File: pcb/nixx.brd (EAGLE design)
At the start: 20 x 40 mm, 42 parts

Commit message: added eeprom
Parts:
- added IC1: 24C64ST, joyAnalog:TSSOP8
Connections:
- new net VCC: IC1.8
- net GND: now also IC1.4
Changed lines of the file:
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@@
 <grid distance="5" unitdist="mil" unit="mm" style="lines" multiple="1" display="no" altdistance="1" altunitdist="mil" altunit="mil"/>
 <layers>
-<layer number="1" name="Top" color="4" fill="1" visible="yes" active="yes"/>
+<layer number="1" name="Top" color="4" fill="1" visible="no" active="yes"/>
 <layer number="16" name="Bottom" color="1" fill="1" visible="yes" active="yes"/>
 <layer number="17" name="Pads" color="2" fill="1" visible="yes" active="yes"/>
@@
 <layer number="21" name="tPlace" color="7" fill="1" visible="yes" active="yes"/>
 <layer number="22" name="bPlace" color="7" fill="1" visible="yes" active="yes"/>
-<layer number="23" name="tOrigins" color="15" fill="1" visible="yes" active="yes"/>
+<layer number="23" name="tOrigins" color="15" fill="1" visible="no" active="yes"/>
 <layer number="24" name="bOrigins" color="15" fill="1" visible="yes" active="yes"/>
-<layer number="25" name="tNames" color="7" fill="1" visible="yes" active="yes"/>
+<layer number="25" name="tNames" color="7" fill="1" visible="no" active="yes"/>
 <layer number="26" name="bNames" color="7" fill="1" visible="yes" active="yes"/>
-<layer number="27" name="tValues" color="7" fill="1" visible="yes" active="yes"/>
+<layer number="27" name="tValues" color="7" fill="1" visible="no" active="yes"/>
 <layer number="28" name="bValues" color="7" fill="1" visible="yes" active="yes"/>
 <layer number="29" name="tStop" color="7" fill="3" visible="no" active="yes"/>
@@
 <layer number="49" name="Reference" color="7" fill="1" visible="yes" active="yes"/>
 <layer number="50" name="dxf" color="7" fill="1" visible="yes" active="yes"/>
-<layer number="51" name="tDocu" color="7" fill="1" visible="yes" active="yes"/>
+<layer number="51" name="tDocu" color="7" fill="1" visible="no" active="yes"/>
 <layer number="52" name="bDocu" color="7" fill="1" visible="yes" active="yes"/>
 <layer number="53" name="tGND_GNDA" color="7" fill="1" visible="yes" active="yes"/>
@@
 <attribute name="VALUE" x="7.239" y="10.287" size="0.4064" layer="28" rot="MR180"/>
 </element>
+<element name="IC1" library="joyAnalog" package="TSSOP8" value="24C64ST" x="9.398" y="8.509" rot="MR0">
+<attribute name="MPN" value="CAT24C64YI-GT3" x="9.398" y="8.509" size="1.778" layer="28" rot="MR0" display="off"/>
+<attribute name="OC_FARNELL" value="1718133" x="9.398" y="8.509" size="1.778" layer="28" rot="MR0" display="off"/>
+<attribute name="OC_NEWARK" value="08R5418" x="9.398" y="8.509" size="1.778" layer="28" rot="MR0" display="off"/>
+<attribute name="MF" value="" x="9.398" y="8.509" size="1.778" layer="28" rot="MR0" display="off"/>
+</element>
 </elements>
 <signals>
@@
 <wire x1="9.155" y1="8.89" x2="10.171" y2="7.874" width="0.2032" layer="16"/>
 <wire x1="10.171" y1="7.874" x2="10.414" y2="7.874" width="0.2032" layer="16"/>
+<contactref element="IC1" pad="4"/>
+<wire x1="10.171" y1="7.874" x2="8.423" y2="5.584" width="0" layer="19" extent="16-16"/>
 </signal>
 <signal name="N$1">
@@
 <wire x1="0.7366" y1="34.6456" x2="1.27" y2="34.1122" width="0.2032" layer="1"/>
 <wire x1="1.27" y1="34.1122" x2="1.27" y2="33.412" width="0.2032" layer="1"/>
+<wire x1="7.355" y1="8.89" x2="12.573" y2="8.255" width="0" layer="19" extent="16-16"/>
 </signal>
 <signal name="SPI_SCK">
@@
 <wire x1="4.215" y1="11.581" x2="5.7074" y2="11.581" width="0.2032" layer="1"/>
 </signal>
+<signal name="VCC">
+<contactref element="IC1" pad="8"/>
+</signal>
 </signals>

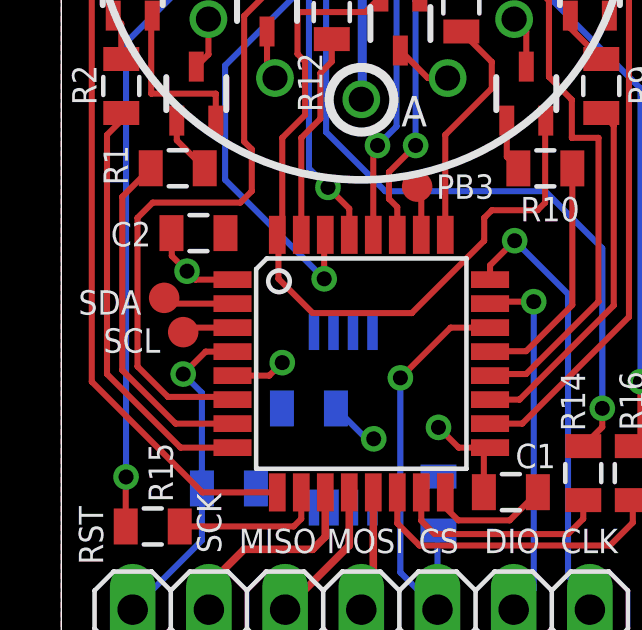
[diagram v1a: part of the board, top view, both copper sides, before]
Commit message: added eeprom
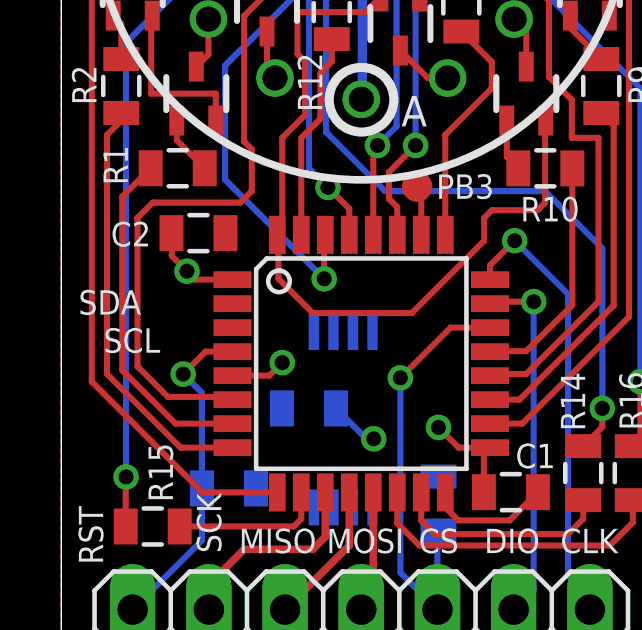
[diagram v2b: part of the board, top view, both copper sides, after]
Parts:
- removed TP1, TP2: TEST-POINT3X4, joyAnalog:PAD.03X.04
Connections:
- removed net N$16: TP1.P$1, U$2.2
- removed net N$18: TP2.P$1, U$2.3
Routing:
- net N$16: track 2.36 -> 0.00 mm
- net N$18: track 1.71 -> 0.00 mm
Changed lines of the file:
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@@
 <attribute name="VALUE" x="17.653" y="7.747" size="0.4064" layer="27" rot="R270"/>
 </element>
-<element name="TP1" library="joyAnalog" package="PAD.03X.04" value="TEST-POINT3X4" x="3.429" y="12.573" smashed="yes"/>
-<element name="TP2" library="joyAnalog" package="PAD.03X.04" value="TEST-POINT3X4" x="4.064" y="11.43" smashed="yes"/>
 <element name="TP3" library="joyAnalog" package="PAD.03X.04" value="TEST-POINT3X4" x="11.8618" y="16.2814" smashed="yes"/>
 <element name="R17" library="joyAnalog" package="0805" value="" x="5.588" y="6.223" smashed="yes" rot="MR180">
@@
 <wire x1="10.795" y1="16.129" x2="8.8265" y2="18.0975" width="0.2032" layer="16"/>
 </signal>
-<signal name="N$16">
-<contactref element="TP1" pad="P$1"/>
-<contactref element="U$2" pad="2"/>
-<wire x1="5.7074" y1="12.381" x2="3.621" y2="12.381" width="0.2032" layer="1"/>
-<wire x1="3.621" y1="12.381" x2="3.429" y2="12.573" width="0.2032" layer="1"/>
-</signal>
-<signal name="N$18">
-<contactref element="TP2" pad="P$1"/>
-<contactref element="U$2" pad="3"/>
-<wire x1="4.064" y1="11.43" x2="4.215" y2="11.581" width="0.2032" layer="1"/>
-<wire x1="4.215" y1="11.581" x2="5.7074" y2="11.581" width="0.2032" layer="1"/>
-</signal>
 <signal name="VCC">

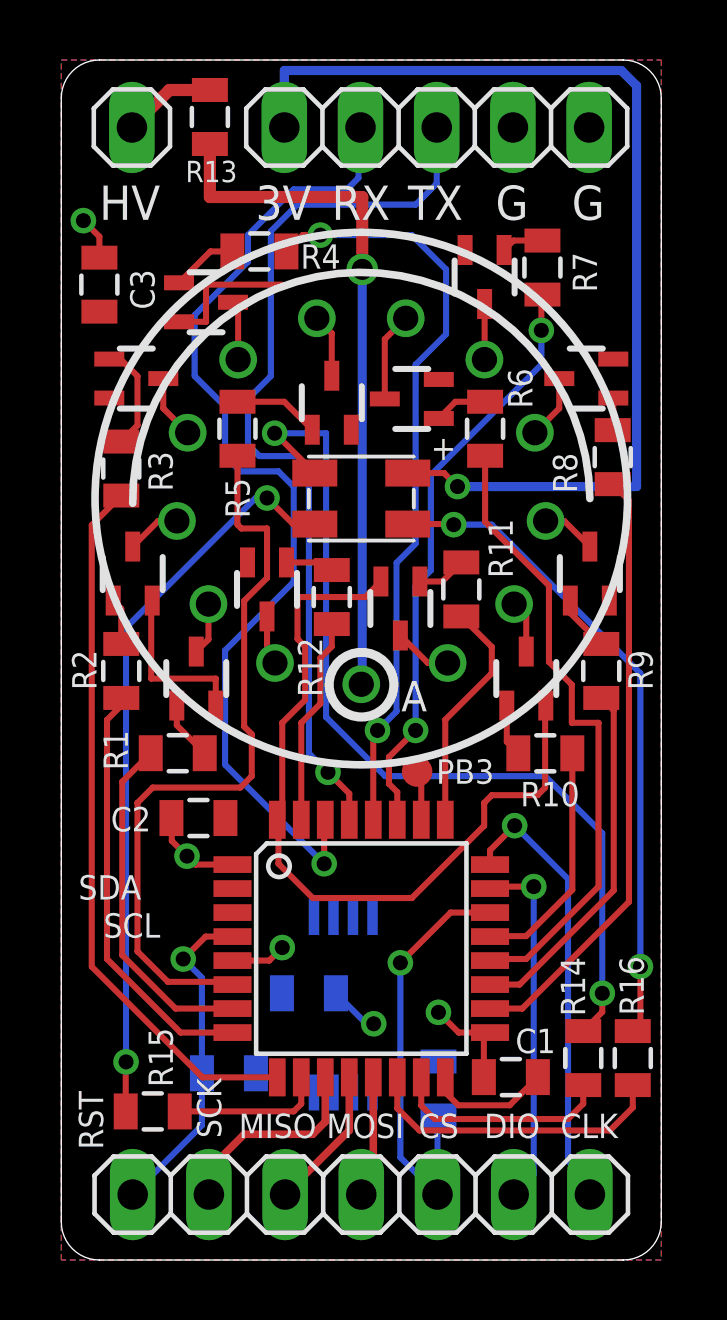
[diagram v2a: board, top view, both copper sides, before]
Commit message: added eeprom
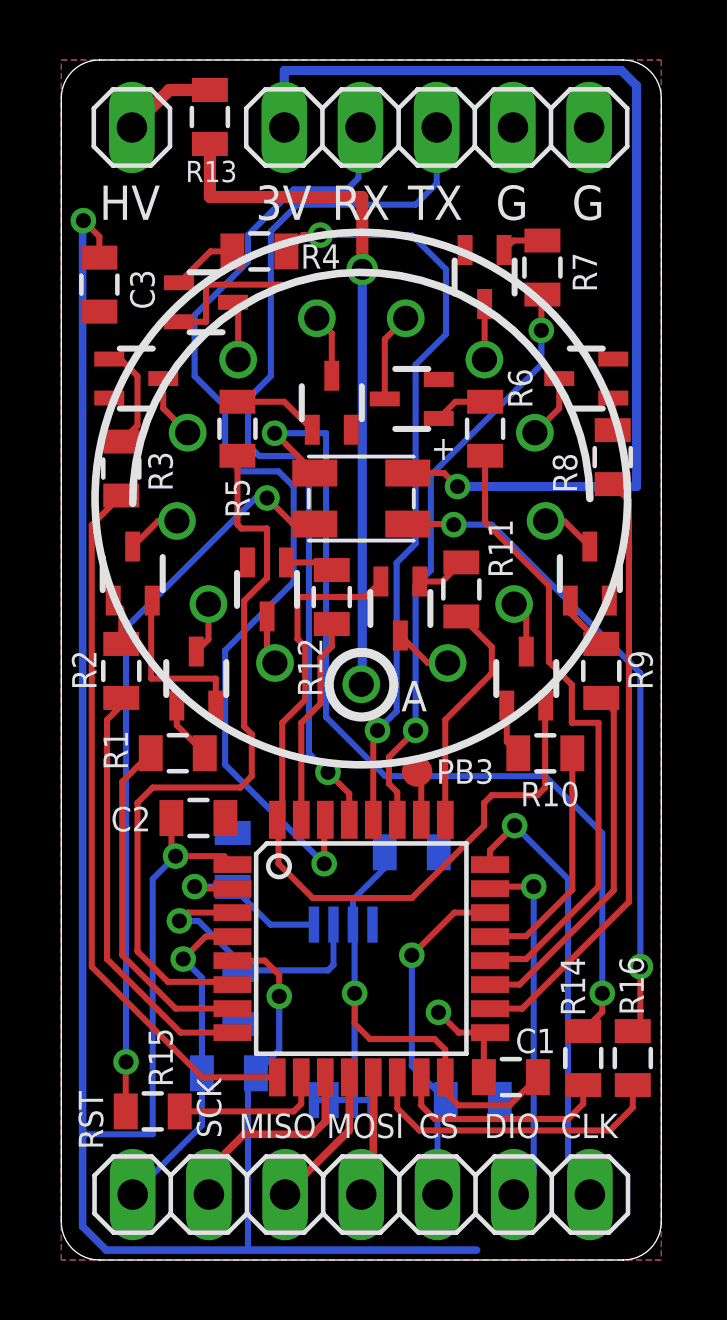
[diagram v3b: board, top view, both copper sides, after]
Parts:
- added R19, R20: (no value), joyAnalog:0805
- moved C4 5.82 mm to (11.7, 13.6), turned to 0 degrees
- moved R18 1.20 mm to (13.7, 5.33), turned to 180 degrees
- moved IC1 0.25 mm to (9.40, 8.26)
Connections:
- removed net VCC: IC1.8
- new net N$16: IC1.5, R20.1, U$2.2
- new net N$18: IC1.6, R19.1, U$2.3
- net +3V3: now also IC1.8, R19.2, R20.2
- net GND: now also IC1.1, IC1.2, IC1.3, IC1.7
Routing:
- net +3V3: track 45.0 -> 113.8 mm
- net GND: track 42.7 -> 57.0 mm
- net N$18: track 0.00 -> 9.27 mm, vias 0 -> 1
- net N$16: track 0.00 -> 5.99 mm, vias 0 -> 1
- net SPI_CS: track 14.6 -> 11.8 mm
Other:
- board text removed: "SCL"
- board text removed: "SDA"

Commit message: added eeprom
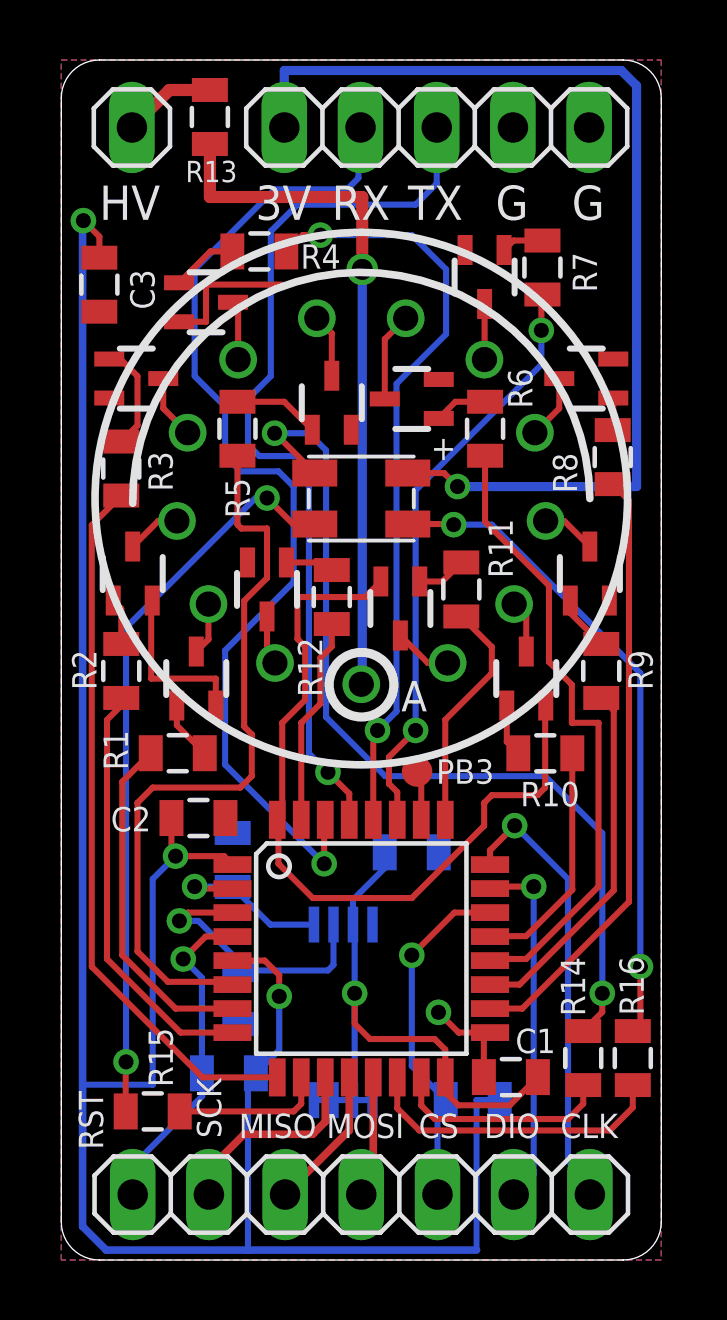
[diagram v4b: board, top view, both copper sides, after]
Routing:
- net +3V3: track 113.8 -> 117.9 mm
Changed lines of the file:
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@@
 <grid distance="5" unitdist="mil" unit="mil" style="lines" multiple="1" display="no" altdistance="1" altunitdist="mil" altunit="mil"/>
 <layers>
-<layer number="1" name="Top" color="4" fill="1" visible="no" active="yes"/>
+<layer number="1" name="Top" color="4" fill="1" visible="yes" active="yes"/>
 <layer number="16" name="Bottom" color="1" fill="1" visible="yes" active="yes"/>
 <layer number="17" name="Pads" color="2" fill="1" visible="yes" active="yes"/>
@@
 <layer number="19" name="Unrouted" color="6" fill="1" visible="yes" active="yes"/>
 <layer number="20" name="Dimension" color="15" fill="1" visible="yes" active="yes"/>
-<layer number="21" name="tPlace" color="7" fill="1" visible="yes" active="yes"/>
+<layer number="21" name="tPlace" color="7" fill="1" visible="no" active="yes"/>
 <layer number="22" name="bPlace" color="7" fill="1" visible="yes" active="yes"/>
 <layer number="23" name="tOrigins" color="15" fill="1" visible="no" active="yes"/>
@@
 <element name="TP3" library="joyAnalog" package="PAD.03X.04" value="TEST-POINT3X4" x="11.8618" y="16.2814" smashed="yes"/>
 <element name="R17" library="joyAnalog" package="0805" value="" x="5.588" y="6.223" smashed="yes" rot="MR180">
-<attribute name="NAME" x="4.7244" y="5.0927" size="0.8128" layer="26" rot="MR180"/>
+<attribute name="NAME" x="4.7244" y="5.2197" size="0.8128" layer="26" rot="MR180"/>
 <attribute name="VALUE" x="4.572" y="7.62" size="0.4064" layer="28" rot="MR180"/>
 <attribute name="VALUE" x="4.572" y="7.62" size="0.4064" layer="28" rot="MR180"/>
@@
 <wire x1="1.4986" y1="0.3302" x2="0.7112" y2="1.1176" width="0.254" layer="16"/>
 <wire x1="0.7112" y1="1.1176" x2="0.7112" y2="4.318" width="0.254" layer="16"/>
-<wire x1="0.7112" y1="4.318" x2="0.7112" y2="34.6202" width="0.254" layer="16"/>
+<wire x1="0.7112" y1="4.318" x2="0.7112" y2="5.842" width="0.254" layer="16"/>
+<wire x1="0.7112" y1="5.842" x2="0.7112" y2="34.6202" width="0.254" layer="16"/>
 <wire x1="0.7112" y1="34.6202" x2="0.7366" y2="34.6456" width="0.254" layer="16"/>
 <wire x1="5.7074" y1="13.181" x2="5.4264" y2="13.462" width="0.2032" layer="1"/>
@@
 <wire x1="6.223" y1="5.958" x2="6.223" y2="0.3302" width="0.2032" layer="16"/>
 <wire x1="3.81" y1="13.462" x2="3.048" y2="12.7" width="0.2032" layer="16"/>
-<wire x1="3.048" y1="12.7" x2="3.048" y2="4.191" width="0.2032" layer="16"/>
-<wire x1="3.048" y1="4.191" x2="0.7112" y2="4.191" width="0.2032" layer="16"/>
 <wire x1="0.7112" y1="4.191" x2="0.7112" y2="4.318" width="0.2032" layer="16"/>
+<wire x1="3.048" y1="12.7" x2="3.048" y2="5.842" width="0.2032" layer="16"/>
+<wire x1="3.048" y1="5.842" x2="0.7112" y2="5.842" width="0.2032" layer="16"/>
+<wire x1="14.616" y1="5.334" x2="13.843" y2="5.334" width="0.2032" layer="16"/>
+<wire x1="13.843" y1="5.334" x2="13.843" y2="0.3302" width="0.2032" layer="16"/>
 </signal>
 <signal name="SPI_SCK">
@@
 <contactref element="R17" pad="1"/>
 <wire x1="4.688" y1="9.409" x2="4.688" y2="6.223" width="0.2032" layer="16"/>
-<wire x1="4.688" y1="6.223" x2="4.688" y2="4.489" width="0.2032" layer="16"/>
-<wire x1="4.688" y1="4.489" x2="2.38" y2="2.181" width="0.2032" layer="16"/>
 <wire x1="5.7074" y1="10.781" x2="4.812" y2="10.781" width="0.2032" layer="1"/>
 <wire x1="4.812" y1="10.781" x2="4.064" y2="10.033" width="0.2032" layer="1"/>
 <wire x1="4.688" y1="9.409" x2="4.064" y2="10.033" width="0.2032" layer="16"/>
+<wire x1="2.38" y1="2.181" x2="2.38" y2="3.142" width="0.2032" layer="16"/>
+<wire x1="2.38" y1="3.142" x2="4.699" y2="5.461" width="0.2032" layer="16"/>
+<wire x1="4.699" y1="5.461" x2="4.699" y2="6.212" width="0.2032" layer="16"/>
+<wire x1="4.699" y1="6.212" x2="4.688" y2="6.223" width="0.2032" layer="16"/>
 </signal>
 <signal name="UART_RX">
@@
 <wire x1="5.461" y1="28.448" x2="4.445" y2="29.464" width="0.2032" layer="16"/>
 <contactref element="JP1" pad="4"/>
-<wire x1="4.445" y1="29.464" x2="4.445" y2="31.496" width="0.2032" layer="16"/>
-<wire x1="4.445" y1="31.496" x2="6.223" y2="33.274" width="0.2032" layer="16"/>
-<wire x1="6.223" y1="33.274" x2="6.223" y2="34.163" width="0.2032" layer="16"/>
-<wire x1="6.223" y1="34.163" x2="7.747" y2="35.687" width="0.2032" layer="16"/>
-<wire x1="7.747" y1="35.687" x2="9.525" y2="35.687" width="0.2032" layer="16"/>
+<wire x1="4.445" y1="29.464" x2="4.445" y2="33.02" width="0.2032" layer="16"/>
+<wire x1="7.112" y1="35.687" x2="9.525" y2="35.687" width="0.2032" layer="16"/>
 <wire x1="9.525" y1="35.687" x2="9.906" y2="36.068" width="0.2032" layer="16"/>
 <wire x1="9.906" y1="36.068" x2="9.906" y2="37.6822" width="0.2032" layer="16"/>
 <wire x1="9.906" y1="37.6822" x2="9.9746" y2="37.7508" width="0.2032" layer="16"/>
+<wire x1="7.112" y1="35.687" x2="4.445" y2="33.02" width="0.2032" layer="16"/>
 </signal>
 <signal name="UART_TX">
@@
 <contactref element="U$2" pad="27"/>
 <via x="11.811" y="17.653" extent="1-16" drill="0.5"/>
-<wire x1="11.811" y1="17.653" x2="11.811" y2="22.479" width="0.2032" layer="16"/>
-<wire x1="11.811" y1="22.479" x2="12.319" y2="22.987" width="0.2032" layer="16"/>
+<wire x1="11.811" y1="17.653" x2="11.811" y2="25.654" width="0.2032" layer="16"/>
 <via x="16.002" y="30.988" extent="1-16" drill="0.5"/>
-<wire x1="12.319" y1="22.987" x2="12.319" y2="26.162" width="0.2032" layer="16"/>
-<wire x1="12.319" y1="26.162" x2="16.002" y2="29.845" width="0.2032" layer="16"/>
+<wire x1="11.811" y1="25.654" x2="16.002" y2="29.845" width="0.2032" layer="16"/>
 <wire x1="16.002" y1="29.845" x2="16.002" y2="30.988" width="0.2032" layer="16"/>
 <wire x1="16.038" y1="32.182" x2="16.002" y2="32.146" width="0.2032" layer="1"/>
@@
 <wire x1="10.4" y1="14.6736" x2="10.4" y2="17.512" width="0.2032" layer="1"/>
 <via x="10.541" y="17.653" extent="1-16" drill="0.5"/>
-<wire x1="11.176" y1="18.288" x2="11.176" y2="23.241" width="0.2032" layer="16"/>
-<wire x1="11.176" y1="23.241" x2="11.811" y2="23.876" width="0.2032" layer="16"/>
-<wire x1="11.811" y1="23.876" x2="11.811" y2="29.845" width="0.2032" layer="16"/>
-<wire x1="11.811" y1="29.845" x2="12.827" y2="30.861" width="0.2032" layer="16"/>
+<wire x1="11.176" y1="29.21" x2="12.827" y2="30.861" width="0.2032" layer="16"/>
 <via x="8.636" y="34.163" extent="1-16" drill="0.5"/>
 <wire x1="12.827" y1="30.861" x2="12.827" y2="33.02" width="0.2032" layer="16"/>
@@
 <wire x1="7.503" y1="33.619" x2="8.047" y2="34.163" width="0.2032" layer="1"/>
 <wire x1="8.047" y1="34.163" x2="8.636" y2="34.163" width="0.2032" layer="1"/>
+<wire x1="11.176" y1="18.288" x2="11.176" y2="29.21" width="0.2032" layer="16"/>
 </signal>
 <signal name="STM_3">
@@
 <wire x1="7.112" y1="27.559" x2="7.122" y2="27.559" width="0.2032" layer="1"/>
 <wire x1="7.122" y1="27.559" x2="8.45" y2="26.231" width="0.2032" layer="1"/>
-<wire x1="7.112" y1="27.559" x2="8.8265" y2="27.559" width="0.2032" layer="16"/>
-<wire x1="8.8265" y1="27.559" x2="8.8265" y2="18.0975" width="0.2032" layer="16"/>
 <wire x1="18.034" y1="8.89" x2="18.034" y2="14.224" width="0.2032" layer="16"/>
 <wire x1="18.034" y1="14.224" x2="16.129" y2="16.129" width="0.2032" layer="16"/>
 <wire x1="16.129" y1="16.129" x2="10.795" y2="16.129" width="0.2032" layer="16"/>
 <wire x1="10.795" y1="16.129" x2="8.8265" y2="18.0975" width="0.2032" layer="16"/>
+<wire x1="8.8265" y1="18.0975" x2="8.8265" y2="26.9875" width="0.2032" layer="16"/>
+<wire x1="8.8265" y1="26.9875" x2="8.255" y2="27.559" width="0.2032" layer="16"/>
+<wire x1="8.255" y1="27.559" x2="7.112" y2="27.559" width="0.2032" layer="16"/>
 </signal>
 <signal name="N$16">
